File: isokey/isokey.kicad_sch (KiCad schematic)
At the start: 43 parts, among them J1 PadExp Left, J2 PadExp Right, SW73 RotaryEncoder_Switch, U1 BlackPill_STLINK, U4 TLV73318PDBV

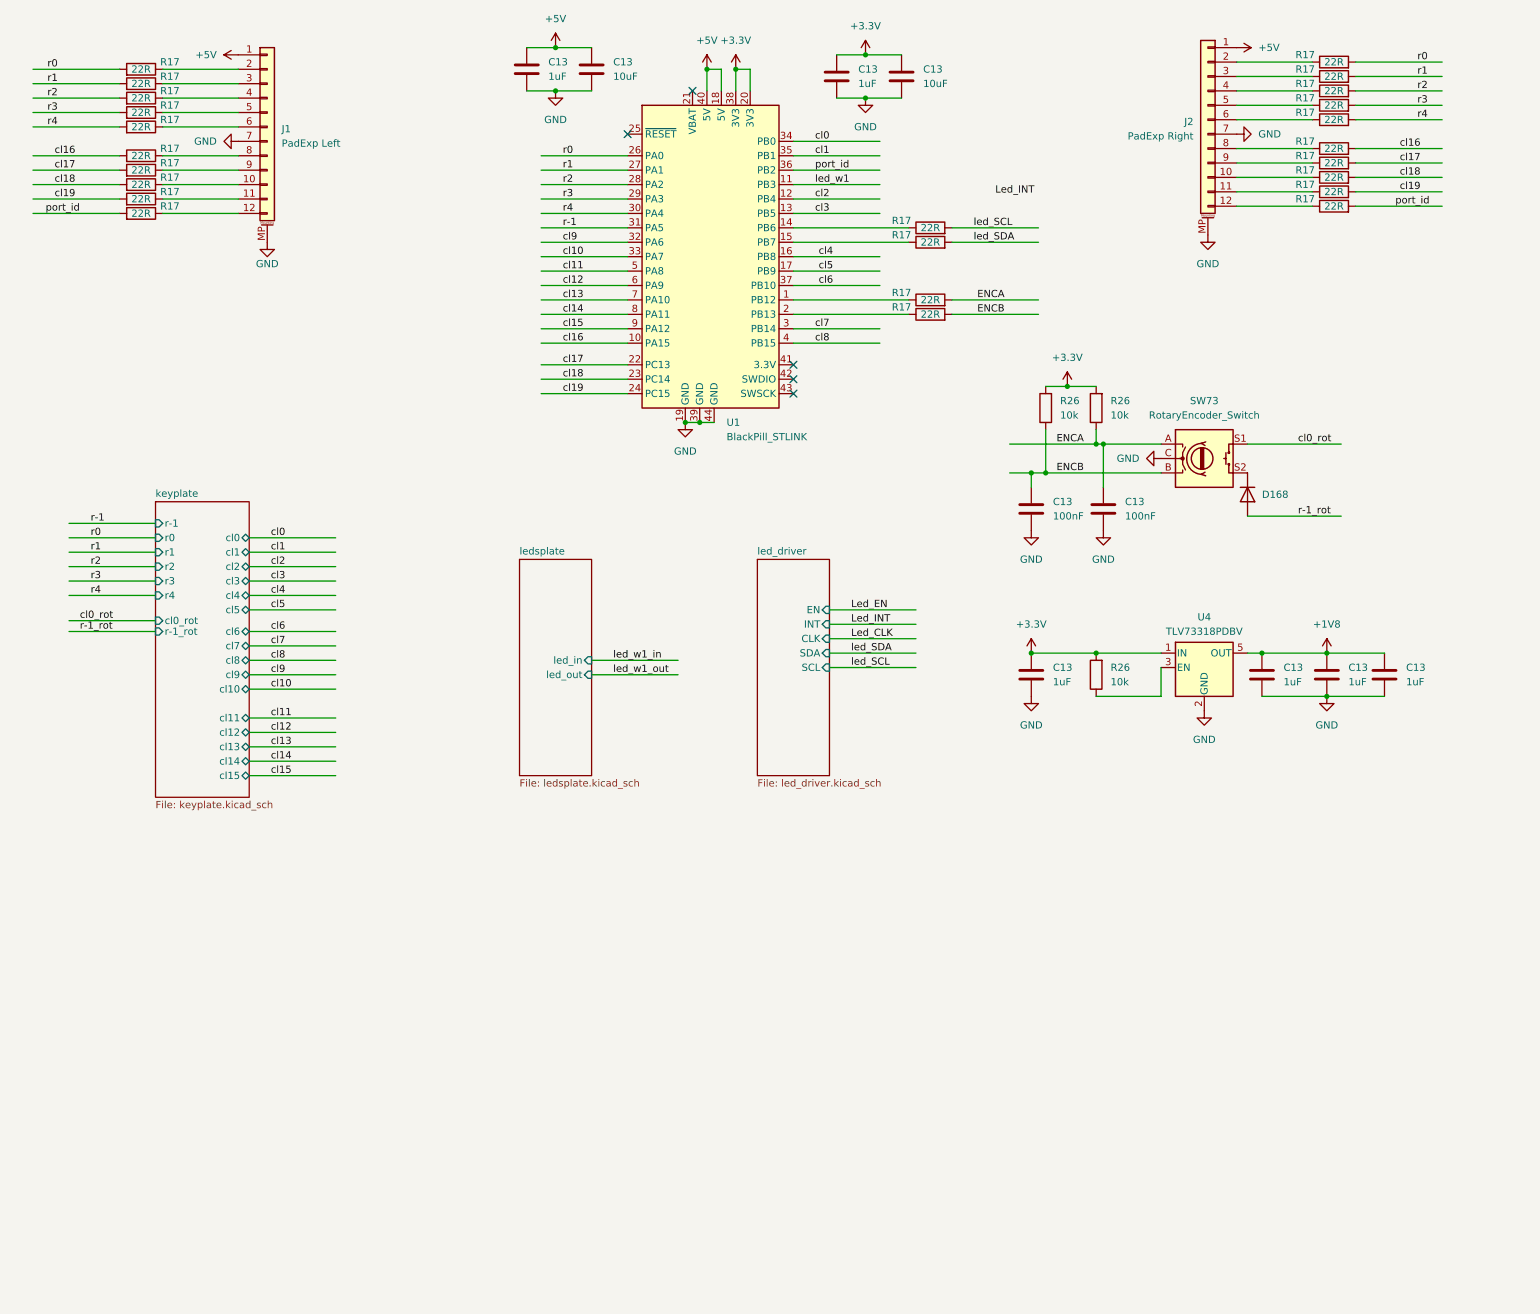
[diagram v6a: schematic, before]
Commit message: Update scheme. Continue routing.
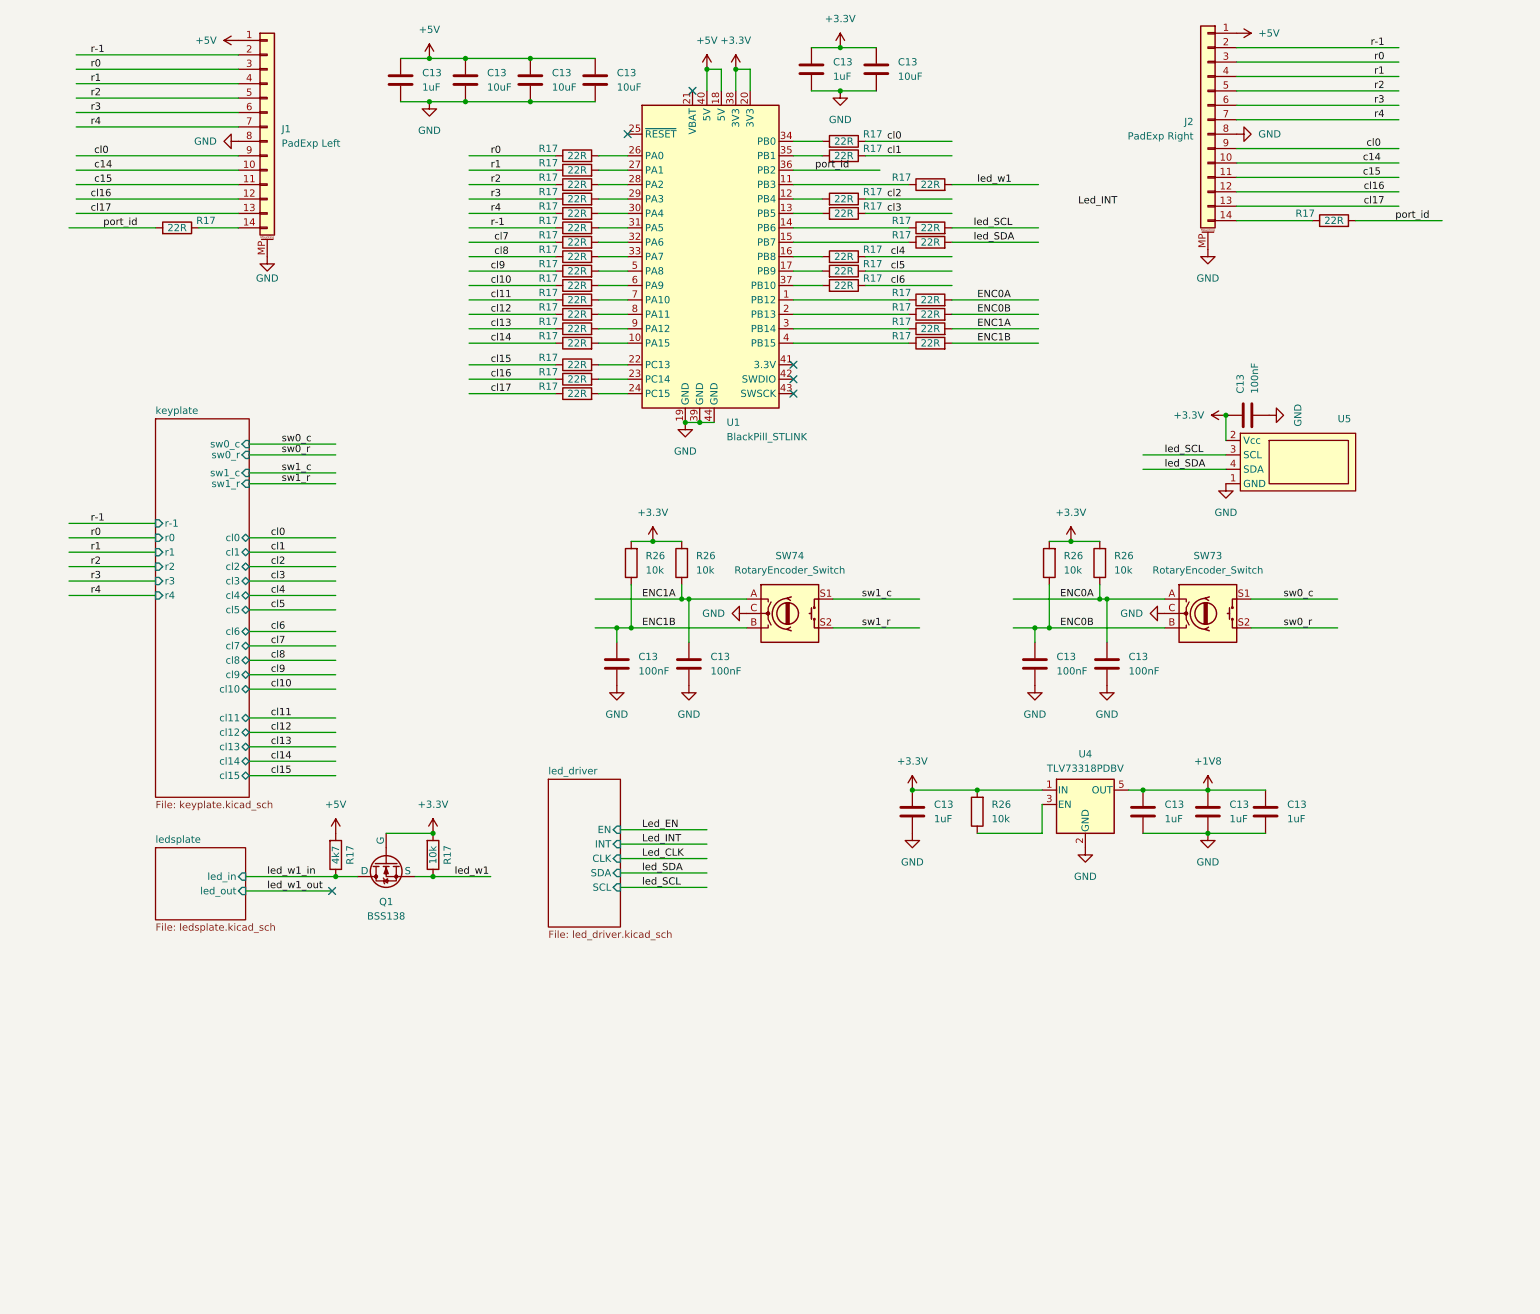
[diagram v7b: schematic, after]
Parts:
- removed D168: 1N4448W, Diode_SMD:D_SOD-123, symbol Diode:1N4448W
- removed R17 (x19): 22R, Resistor_SMD:R_0603_1608Metric_Pad0.98x0.95mm_HandSolder, symbol Device:R
- added C13 (x2): 10uF, Capacitor_SMD:C_1206_3216Metric, symbol Device:C
- added C13 (x3): 100nF, Capacitor_SMD:C_0603_1608Metric_Pad1.08x0.95mm_HandSolder, symbol Device:C
- added Q1: BSS138, Package_TO_SOT_SMD:SOT-23-3, symbol Simulation_SPICE:NMOS
- added R17 (x28): 22R, Resistor_SMD:R_0603_1608Metric_Pad0.98x0.95mm_HandSolder, symbol Device:R
- added R17: 4k7, Resistor_SMD:R_0603_1608Metric_Pad0.98x0.95mm_HandSolder, symbol Device:R
- added R17, R26 (x2): 10k, Resistor_SMD:R_0603_1608Metric_Pad0.98x0.95mm_HandSolder, symbol Device:R
- added SW74: RotaryEncoder_Switch, Rotary_Encoder:RotaryEncoder_Alps_EC12E-Switch_Vertical_H20mm_CircularMountingHoles, symbol Device:RotaryEncoder_Switch
- added U5: ~, Display:OLED_Display_128x32_SSD1306_i2c, symbol Display_Graphic:OLED_Display_128x32_SSD1306_i2c
- J1, J2: footprint Connector_JST:JST_GH_SM12B-GHS-TB_1x12-1MP_P1.25mm_Horizontal -> Connector_JST:JST_GH_SM14B-GHS-TB_1x14-1MP_P1.25mm_Horizontal; symbol Connector_Generic_MountingPin:Conn_01x12_MountingPin -> Connector_Generic_MountingPin:Conn_01x14_MountingPin
- U1: footprint Modules:BlackPill -> Module:BlackPill
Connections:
- net +3.3V: now also C13.1, Q1.2 (G), R17.2, R26.2, R26.2, U5.2 (Vcc)
- net +5V: now also C13.1, C13.1, R17.2
- net GND: now also J1.8 (Pin_8), J2.8 (Pin_8), C13.2, C13.2, C13.2, C13.2, C13.2, SW74.C, U5.1 (GND); no longer J1.7 (Pin_7), J2.7 (Pin_7)
- net cl0: now also J1.9 (Pin_9), J2.9 (Pin_9), R17.1; no longer U1.34 (PB0)
- net cl1: now also R17.1; no longer U1.35 (PB1)
- net cl10: now also R17.1; no longer U1.33 (PA7)
- net cl11: now also R17.1; no longer U1.5 (PA8)
- net cl12: now also R17.1; no longer U1.6 (PA9)
- net cl13: now also R17.1; no longer U1.7 (PA10)
- net cl14: now also R17.1; no longer U1.8 (PA11)
- net cl15: now also R17.1; no longer U1.9 (PA12)
- net cl16: now also J1.12 (Pin_12), J2.12 (Pin_12), R17.1; no longer U1.10 (PA15)
- net cl17: now also J1.13 (Pin_13), J2.13 (Pin_13), R17.1; no longer U1.22 (PC13)
- net cl2: now also R17.1; no longer U1.12 (PB4)
- net cl3: now also R17.1; no longer U1.13 (PB5)
- net cl4: now also R17.1; no longer U1.16 (PB8)
- net cl5: now also R17.1; no longer U1.17 (PB9)
- net cl6: now also R17.1; no longer U1.37 (PB10)
- net cl7: now also R17.1; no longer U1.3 (PB14)
- net cl8: now also R17.1; no longer U1.4 (PB15)
- net cl9: now also R17.1; no longer U1.32 (PA6)
- net led_SCL: now also U5.3 (SCL)
- net led_SDA: now also U5.4 (SDA)
- net led_w1: now also Q1.3 (S), R17.1, R17.2; no longer U1.11 (PB3)
- net led_w1_in: now also Q1.1 (D), R17.1
- net port_id: now also R17.2
- net r-1: now also J1.2 (Pin_2), J2.2 (Pin_2), R17.1; no longer U1.31 (PA5)
- net r0: now also J1.3 (Pin_3), J2.3 (Pin_3), R17.1; no longer U1.26 (PA0)
- net r1: now also J1.4 (Pin_4), J2.4 (Pin_4), R17.1; no longer U1.27 (PA1)
- net r2: now also J1.5 (Pin_5), J2.5 (Pin_5), R17.1; no longer U1.28 (PA2)
- net r3: now also J1.6 (Pin_6), J2.6 (Pin_6), R17.1; no longer U1.29 (PA3)
- net r4: now also J1.7 (Pin_7), J2.7 (Pin_7), R17.1; no longer U1.30 (PA4)
- net at R17.1: now also J2.14 (Pin_14); no longer J2.12 (Pin_12)
- net sw0_r: now reaches SW73.S2
- net c14: now reaches J1.10 (Pin_10)
- net c14: now also J2.10 (Pin_10)
- net c15: now reaches J2.11 (Pin_11)
- net c15: now also J1.11 (Pin_11)
- net ENCA renamed ENC0A
- net ENCB renamed ENC0B
- net cl0_rot renamed sw0_c
- net cl18: no longer names the net of U1.23 (PC14)
- net cl18: now also R17.2
- net cl19: no longer names the net of U1.24 (PC15)
- net cl19: now also R17.2
- new net: R17.2, U1.13 (PB5)
- new net: R17.2, U1.9 (PA12)
- new net: R17.2, U1.26 (PA0)
- new net: R17.2, U1.7 (PA10)
- new net: R17.2, U1.30 (PA4)
- new net: R17.1, U1.4 (PB15)
- new net: R17.2, U1.32 (PA6)
- new net: R17.2, U1.5 (PA8)
- new net: R17.2, U1.31 (PA5)
- new net: R17.1, U1.11 (PB3)
- new net: R17.2, U1.8 (PA11)
- new net: R17.2, U1.37 (PB10)
- new net: J1.14 (Pin_14), R17.1
- new net: R17.2, U1.16 (PB8)
- new net: R17.2, U1.22 (PC13)
- new net: R17.2, U1.35 (PB1)
- new net: R17.2, U1.10 (PA15)
- new net: R17.2, U1.33 (PA7)
- new net: R17.2, U1.28 (PA2)
- new net: R17.2, U1.27 (PA1)
- new net: R17.2, U1.12 (PB4)
- new net: R17.2, U1.17 (PB9)
- new net: R17.2, U1.29 (PA3)
- new net: R17.1, U1.3 (PB14)
- new net: R17.2, U1.34 (PB0)
- new net: R17.2, U1.6 (PA9)
- new net ENC1A: C13.1, R17.2, R26.1, SW74.A
- new net ENC1B: C13.1, R17.2, R26.1, SW74.B
- new net sw1_c: SW74.S1
- new net sw1_r: SW74.S2
- no-connect marks 5 -> 6
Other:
- sheet keyplate ports: added sw0_c, sw0_r, sw1_c, sw1_r; removed cl0_rot, r-1_rot
- moved on the sheet: C13, R17, R26, SW73, U4

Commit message: WIP
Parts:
- added H1, H2, H3, H4: StabilizerHoles, Button_Switch_Keyboard:Stabilizer_MX_2u, symbol Mechanical:MountingHole
- added R25, R27: 10k, Resistor_SMD:R_0603_1608Metric_Pad0.98x0.95mm_HandSolder, symbol Device:R
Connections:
- net sw0_c is gone; now on net cl12: SW73.S1
- net sw1_c is gone; now on net cl6: SW74.S1
- net +3.3V: now also R25.1, R27.1
- net led_SCL: now also R27.2
- net led_SDA: now also R25.2
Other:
- sheet keyplate ports: added none; removed sw0_c, sw1_c
- sheet led_driver ports: added none; removed EN
